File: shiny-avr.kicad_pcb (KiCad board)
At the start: 4 copper layers, 42.2 x 20.3 mm, 32 parts, among them J1 USB_B_Micro, J2 SWD, U1 AMS1117-3.3, U2 STM32F103C6Tx, U3 ATtiny85-20PU, Y1 8 MHz

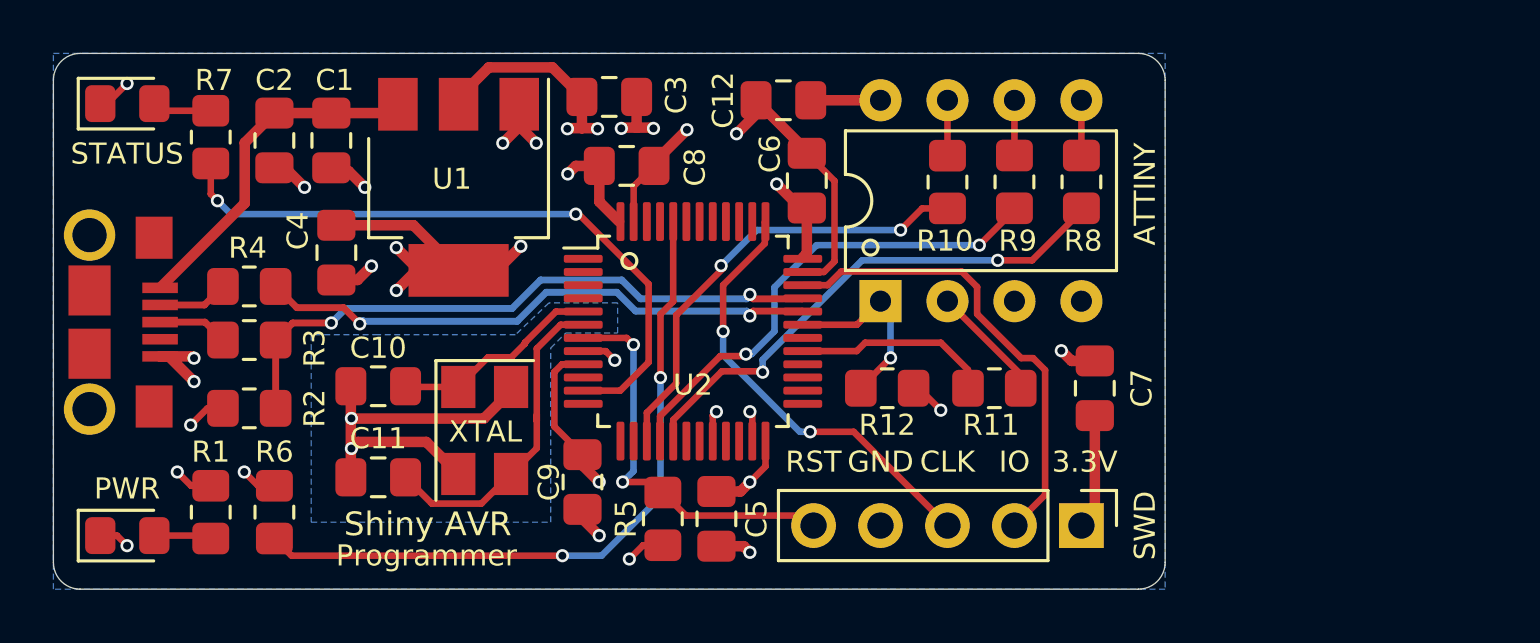
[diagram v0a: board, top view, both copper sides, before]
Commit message: Add support for ATtiny24/44/48 (#2)
* feat: Add support for ATtinyx4

* fix

Co-authored-by: Tibor Djurica Potpara <tibor.djurica@reddit.com>
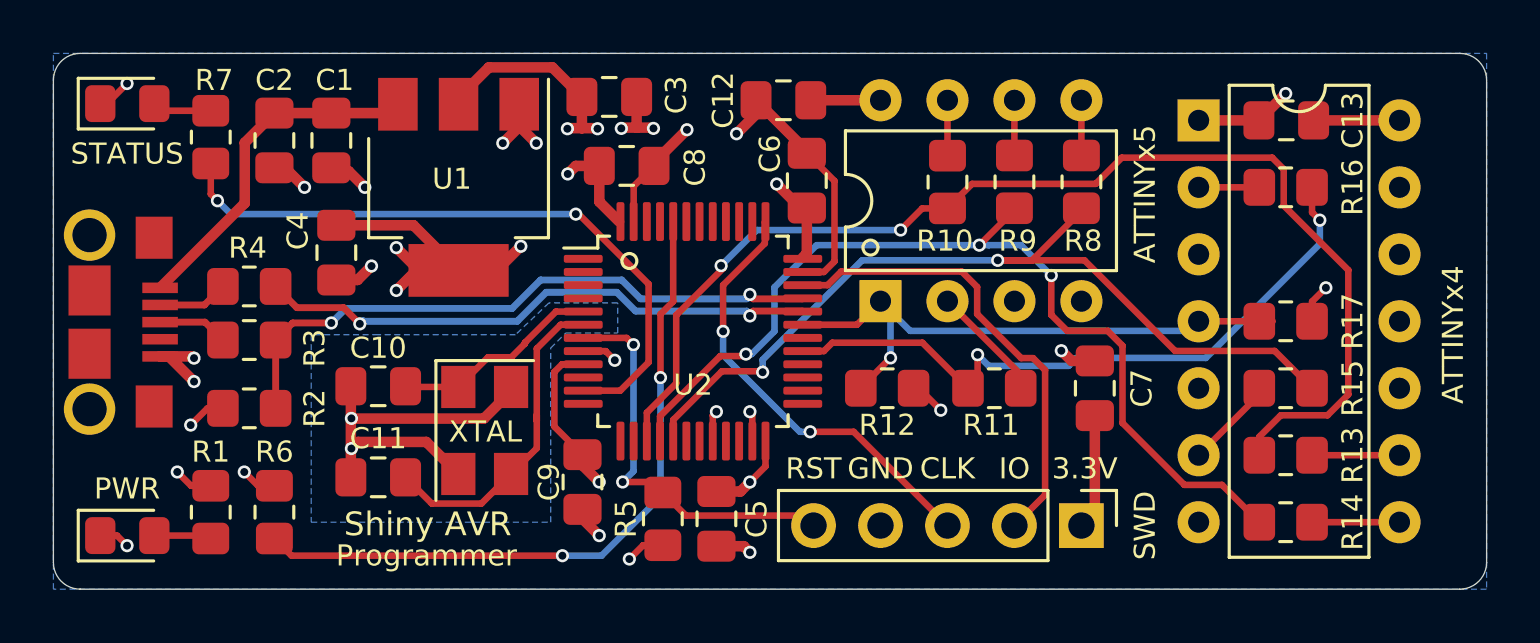
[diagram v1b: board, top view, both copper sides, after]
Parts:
- added C13: 100n, Capacitor_SMD:C_0805_2012Metric_Pad1.18x1.45mm_HandSolder, F.Cu at (176.8, 99.1)
- added R13: 1k, Resistor_SMD:R_0805_2012Metric_Pad1.20x1.40mm_HandSolder, F.Cu at (176.8, 111.8)
- added R14: 1k, Resistor_SMD:R_0805_2012Metric_Pad1.20x1.40mm_HandSolder, F.Cu at (176.8, 114.3)
- added R15: 1k, Resistor_SMD:R_0805_2012Metric_Pad1.20x1.40mm_HandSolder, F.Cu at (176.8, 109.2)
- added R16: 1k, Resistor_SMD:R_0805_2012Metric_Pad1.20x1.40mm_HandSolder, F.Cu at (176.8, 101.6)
- added R17: 10k, Resistor_SMD:R_0805_2012Metric_Pad1.20x1.40mm_HandSolder, F.Cu at (176.8, 106.7)
- added U4: ATtiny85-20PU, Package_DIP:DIP-14_W7.62mm, F.Cu at (173.5, 99.1)
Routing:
- net ISP_CLK: track 17.4 -> 45.4 mm
- net EXT_CLOCK: track 7.52 -> 25.9 mm, vias 0 -> 2
- net ISP_MISO: track 18.6 -> 36.2 mm, vias 2 -> 3
- net ISP_RESET: track 7.25 -> 22.7 mm
- net ISP_MOSI: track 19.8 -> 33.7 mm
- net +3V3: track 51.1 -> 56.3 mm, vias 13 -> 15
- net Net-(R15-Pad2): track 0.00 -> 3.49 mm
- net Net-(R14-Pad2): track 0.00 -> 3.32 mm
- net Net-(R13-Pad2): track 0.00 -> 3.32 mm
- net GND: track 58.5 -> 61.8 mm
- net Net-(R16-Pad2): track 0.00 -> 2.30 mm
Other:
- board size 42.2 x 20.3 mm -> 54.4 x 20.3 mm
- board text added: "ATTINYx4"
- board text added: "ATTINYx5"
- board text removed: "ATTINY"
